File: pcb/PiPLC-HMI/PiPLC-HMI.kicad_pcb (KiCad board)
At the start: 2 copper layers, 98 x 50 mm, 23 parts, among them J1 Conn_02x12_Odd_Even, J2 KNX

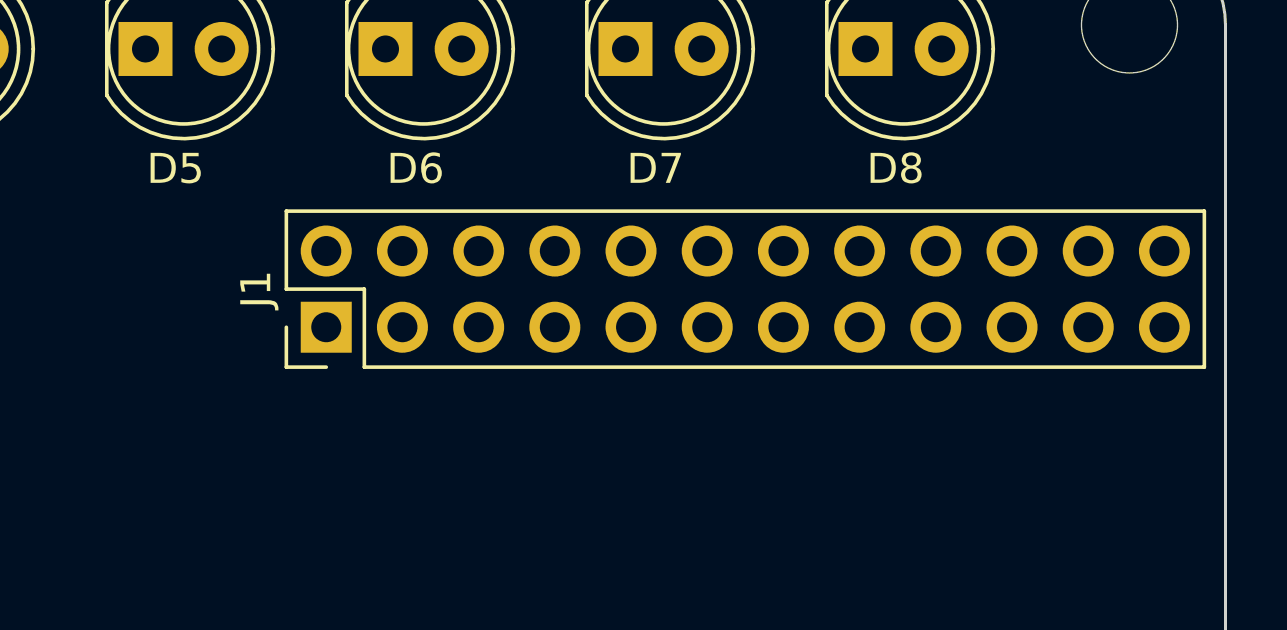
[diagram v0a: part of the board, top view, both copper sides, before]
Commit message: Rename both PCBs and align their connector
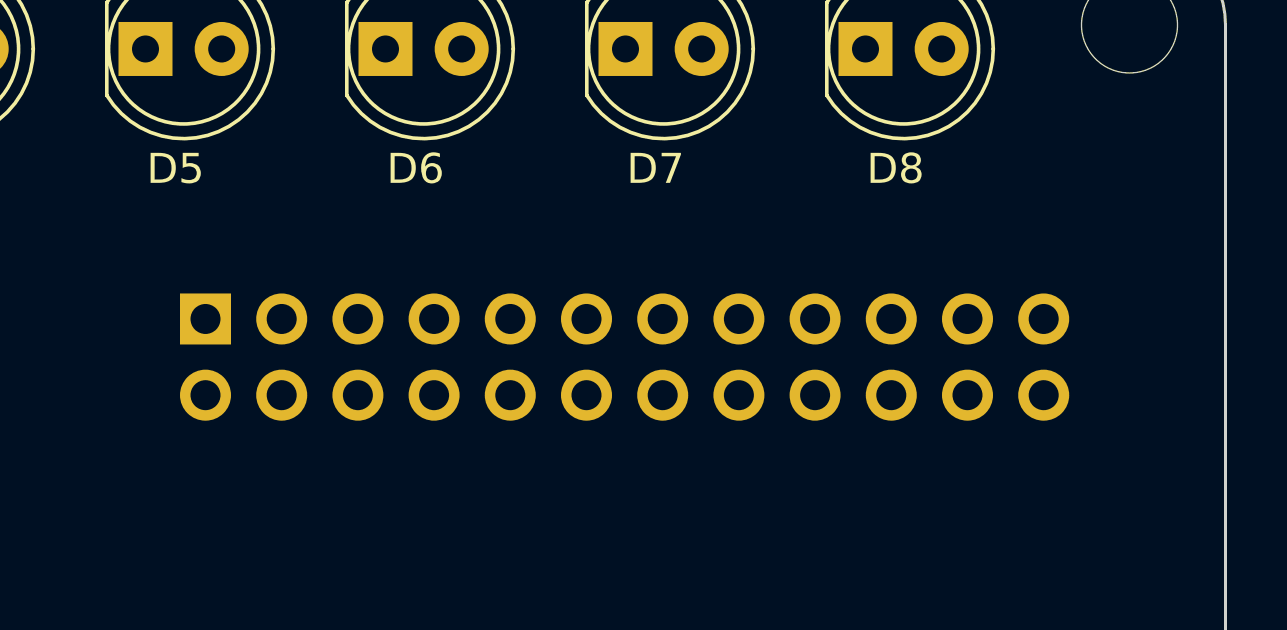
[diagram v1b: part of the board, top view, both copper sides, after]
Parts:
- J1: moved to B.Cu
- moved J1 4.03 mm to (181.9, 79.8), turned to -90 degrees
